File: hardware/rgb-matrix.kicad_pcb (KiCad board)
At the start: 4 copper layers, 58 x 58 mm, 84 parts, among them CON1 VEXT, P1 MATRIX_BOT, P10 PSOUTH, P11 PEAST, P12 WEST, P13 NORTH, P14 SOUTH, P15 EAST, P2 MATRIX_TOP, P3 SWD, P4 SPI3, P5 UART5, P6 VEXT, P7 USB_B, P8 PWEST, P9 PNORTH, SW1 RESET, SW2 BOOT, U1 74AC244, U2 74AC244, U3 74AC244, U4 ULN2803A, U5 STM32F405R, U6 LD3985M33R, U7 USBUF01W6, X1 8MHz

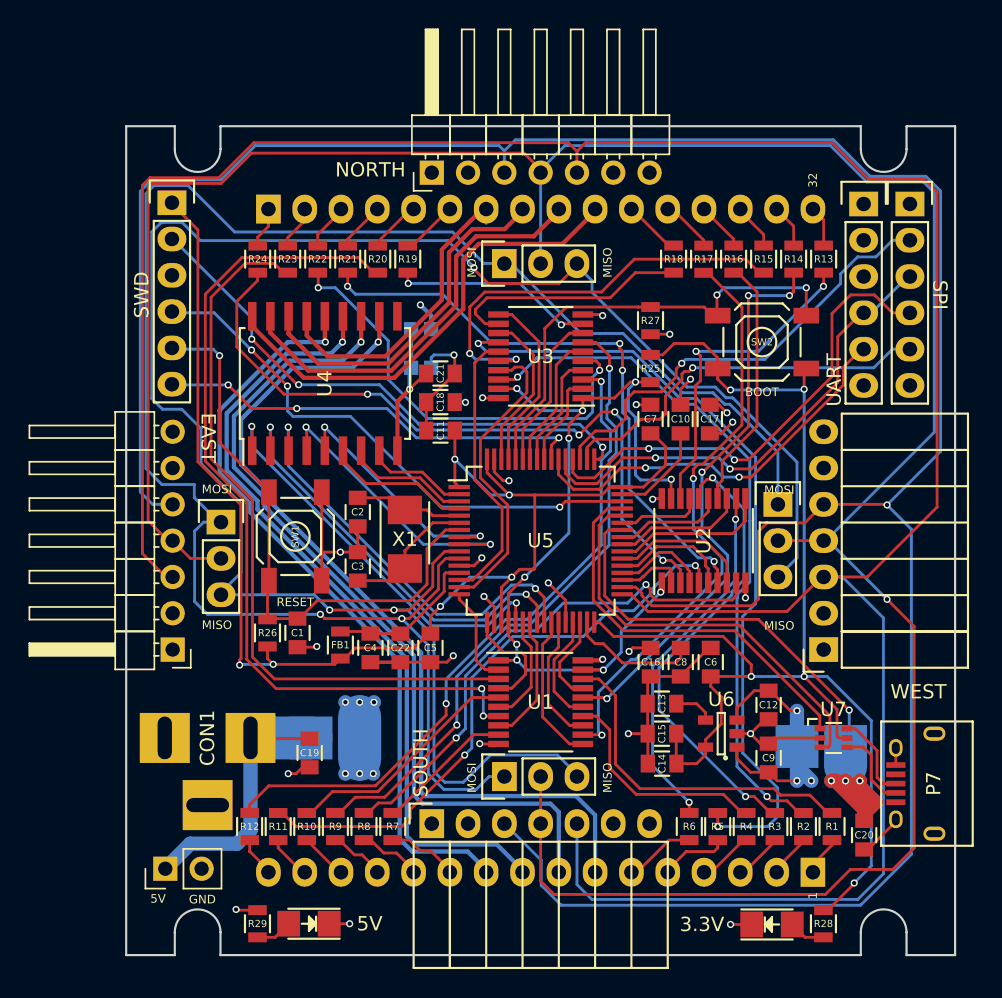
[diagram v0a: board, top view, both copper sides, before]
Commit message: Place vias on pads
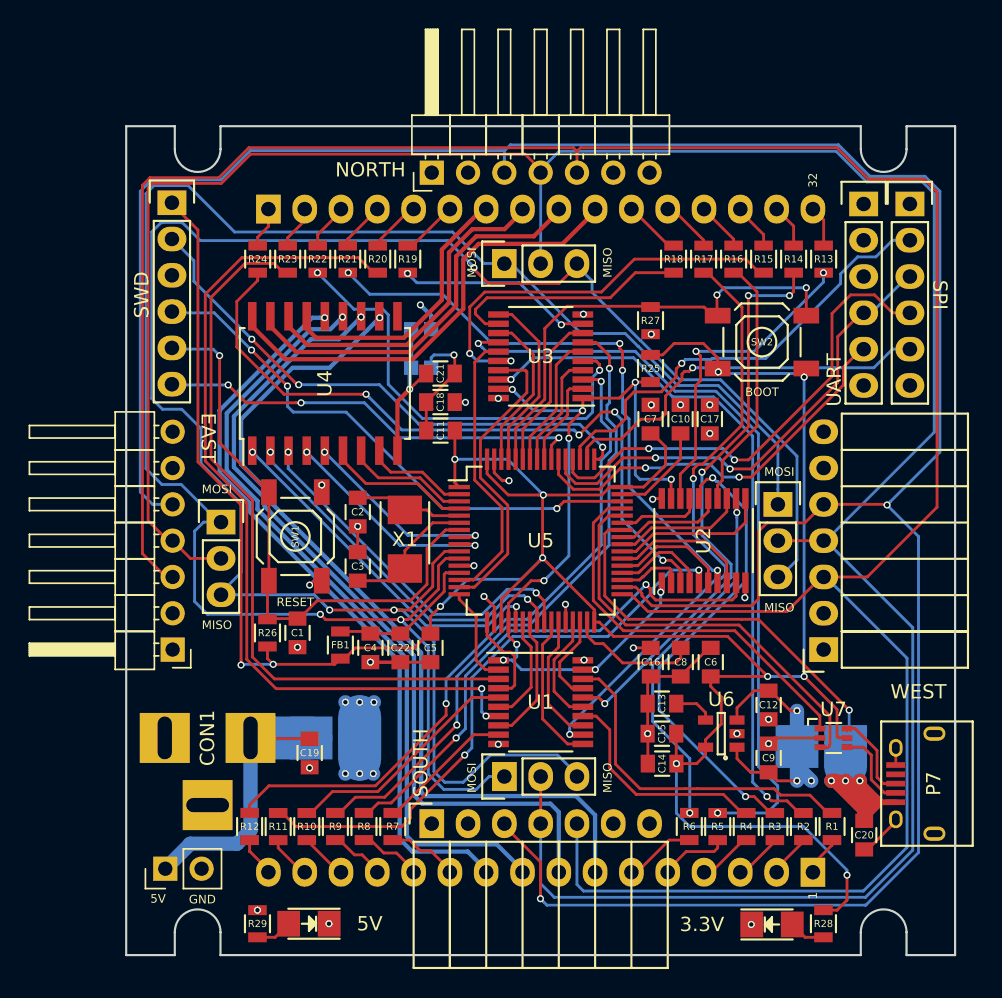
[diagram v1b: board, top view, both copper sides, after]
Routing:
- net GND: track 77.7 -> 45.6 mm, vias 20 -> 24
- net +3V3: track 187.9 -> 200.2 mm, vias 11 -> 12
- net +5V: track 44.7 -> 38.4 mm
- net ON_ROW4: track 20.8 -> 15.7 mm
- net ON_ROW3: track 30.4 -> 25.9 mm
- net ON_ROW5: track 17.9 -> 14.3 mm
- net ON_ROW1: track 28.8 -> 25.3 mm
- net ON_ROW2: track 29.4 -> 26.0 mm
- net ROW4: track 21.8 -> 19.5 mm
- net B3: track 56.1 -> 54.5 mm
- net VBUS: track 45.7 -> 47.1 mm
- net ROW3: track 25.2 -> 23.9 mm
- net ROW2: track 29.4 -> 28.0 mm
- net ROW1: track 33.6 -> 32.5 mm
- net PWM_R2: track 7.79 -> 6.73 mm
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
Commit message: PCB tweaking #1
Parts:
- moved C20 4.84 mm to (181.8, 118.0), turned to 180 degrees
- moved U7 2.83 mm to (183.5, 112.3)
- moved R15 1.85 mm to (175.9, 81.4)
- moved R21 1.85 mm to (150.5, 81.4)
- moved R13 1.85 mm to (180.1, 81.4)
- moved R14 1.85 mm to (178.0, 81.4)
- moved R16 1.85 mm to (173.8, 81.4)
- moved R17 1.85 mm to (171.7, 81.5)
- moved R18 1.85 mm to (169.6, 81.4)
- moved R19 1.85 mm to (154.7, 81.4)
- moved R20 1.85 mm to (152.6, 81.4)
- moved R22 1.85 mm to (148.4, 81.4)
- moved R23 1.85 mm to (146.3, 81.4)
- moved R24 1.85 mm to (144.2, 81.4)
- moved P15 1.24 mm to (139.8, 98.7)
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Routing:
- net +5V: track 38.4 -> 17.6 mm, vias 17 -> 23
- net VBUS: track 47.1 -> 55.0 mm, vias 4 -> 6
- net /mcu/BOOT0: track 32.9 -> 29.2 mm
- net +3V3: track 200.2 -> 196.9 mm
- net R6: track 60.5 -> 63.3 mm
- net G3: track 17.8 -> 20.1 mm, vias 0 -> 2
- net R2: track 40.8 -> 38.5 mm, vias 4 -> 2
- net Net-(P7-Pad3): track 6.26 -> 8.47 mm
- net B4: track 17.1 -> 15.0 mm
- net R4: track 41.7 -> 43.8 mm
- net B2: track 29.6 -> 27.5 mm
- net Net-(P7-Pad2): track 5.75 -> 7.74 mm
- net R8: track 51.0 -> 53.0 mm
- net G8: track 49.7 -> 51.6 mm
- net B7: track 31.3 -> 29.5 mm
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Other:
- board text added: "NRST"
- board text added: "NSS"
- board text added: "RX"
- board text added: "SCK"
- board text added: "SWCLK"
- board text added: "SWDIO"
- board text added: "SWO"
- board text added: "TX"
- board text added: "VDD"

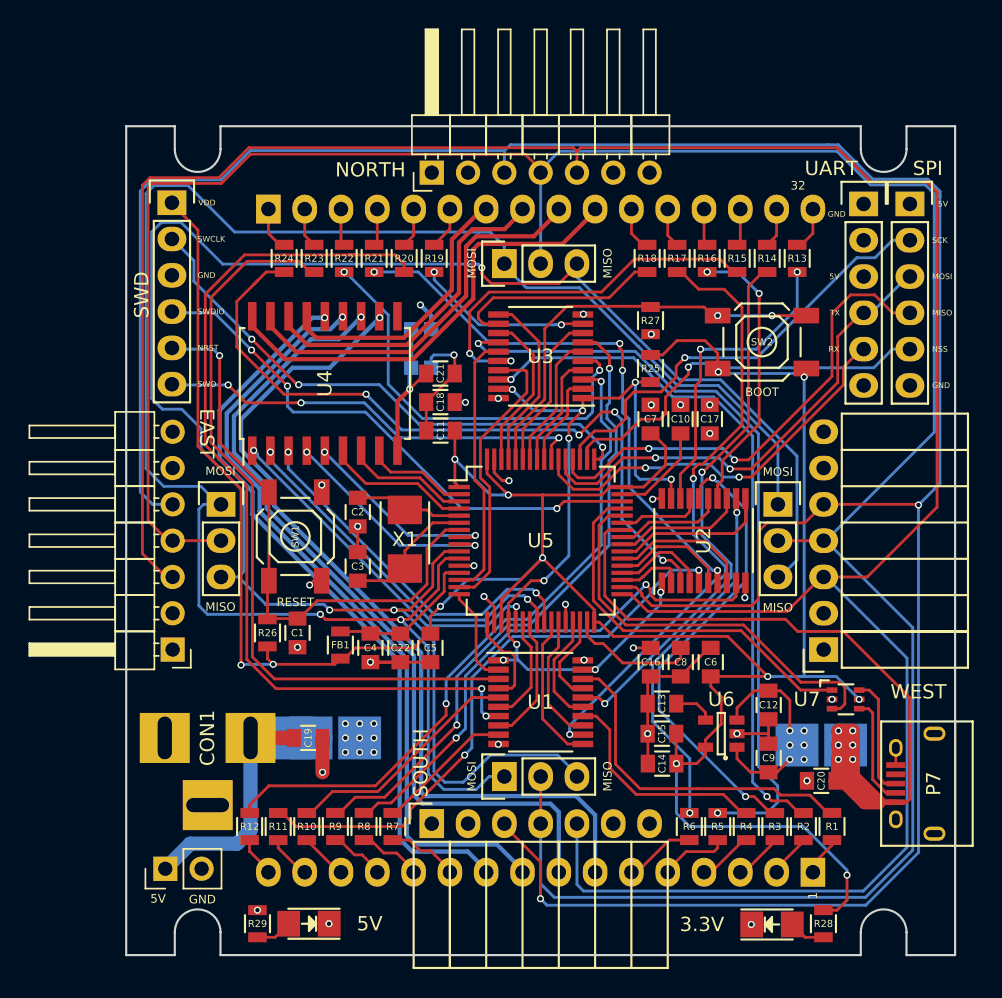
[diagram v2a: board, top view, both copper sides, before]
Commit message: Fix footprint for U7, minor other fixes
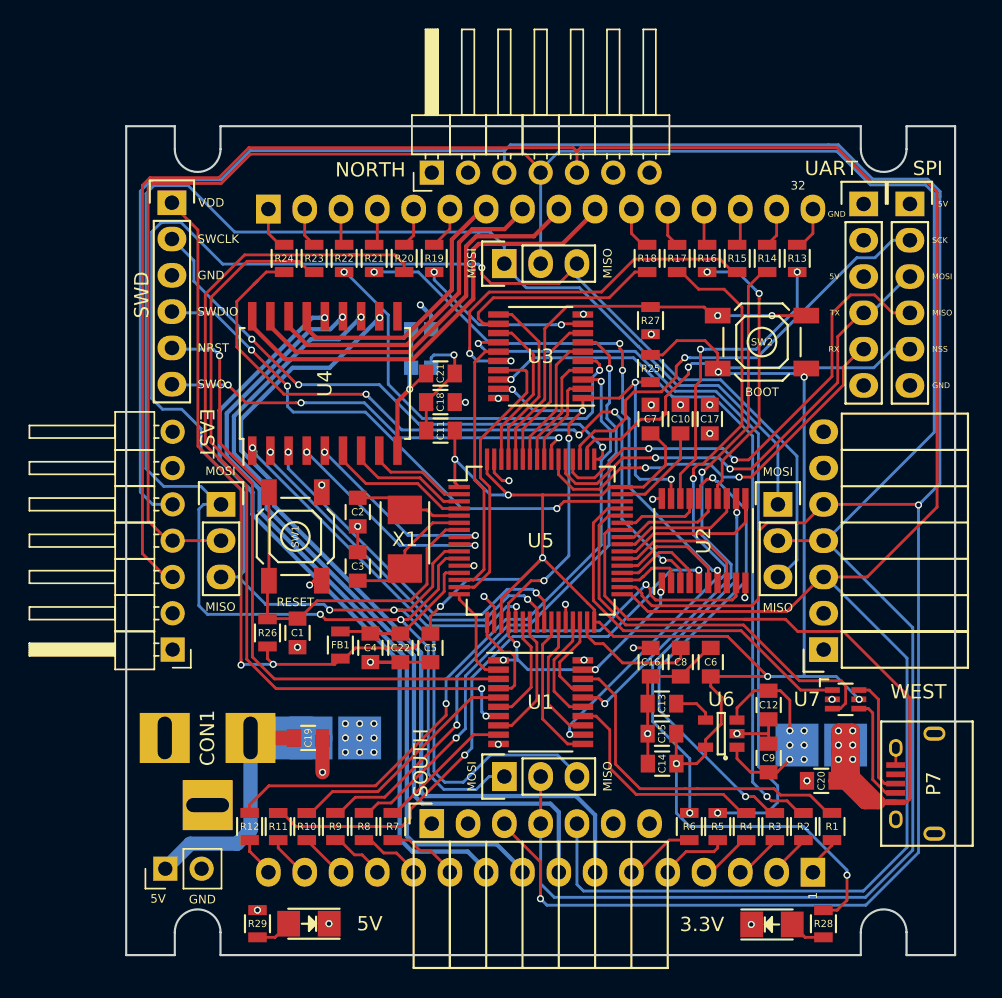
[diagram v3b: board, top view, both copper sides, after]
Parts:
- U7: footprint TO_SOT_Packages_SMD:SC-70-6 -> rgb-matrix:SOT323-6L

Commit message: Fixup silkscreen
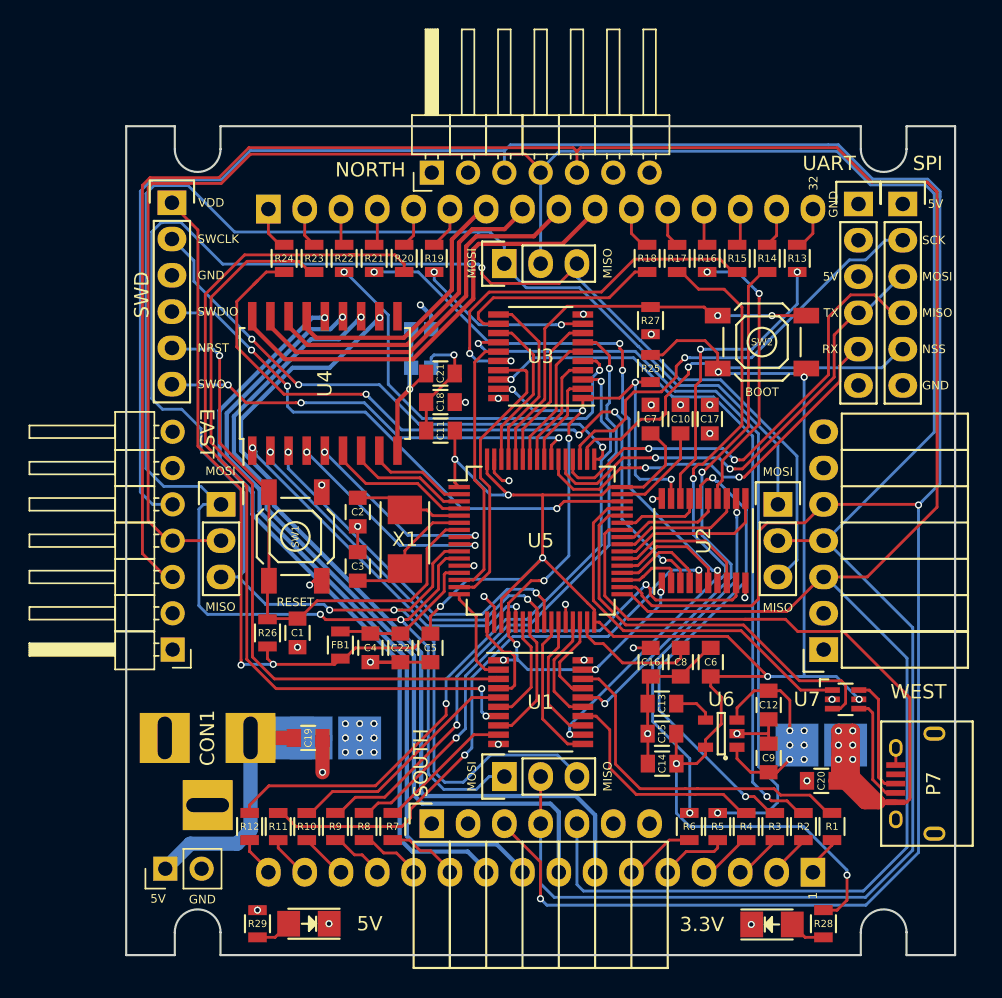
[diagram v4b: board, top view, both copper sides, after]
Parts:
- moved P4 0.50 mm to (187.5, 77.6)
- moved P5 0.36 mm to (184.4, 77.6)
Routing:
- net /mcu/SPI3_SCK: track 31.2 -> 31.9 mm
- net /mcu/SPI3_NSS: track 27.5 -> 27.0 mm
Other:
- board text added: "DATA"

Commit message: Add GND pour to Top and Bottom + via stiching
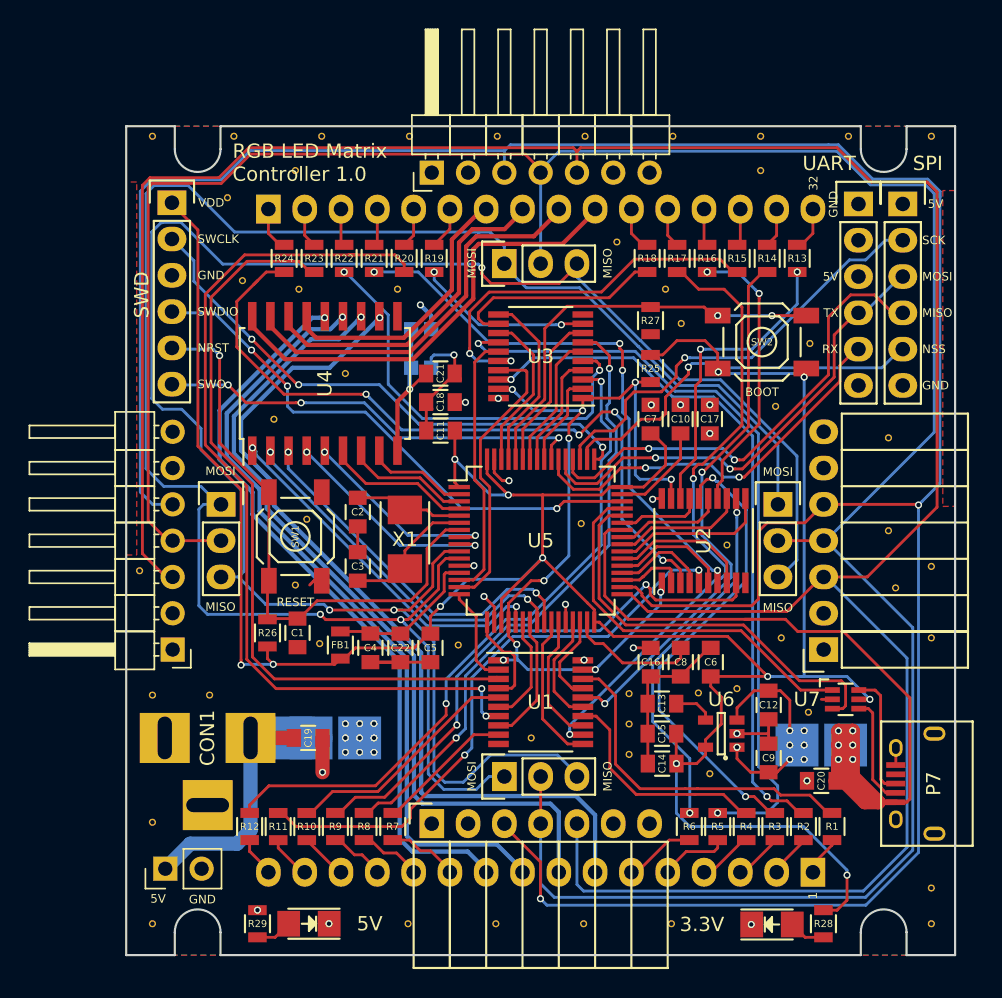
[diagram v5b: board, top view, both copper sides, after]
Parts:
- added REF**: VIA-0.5mm, VIA-0.5mm, F.Cu at (189.5, 125.5)
- added REF**: VIA-0.5mm, VIA-0.5mm, F.Cu at (181.0, 87.4)
- added REF**: VIA-0.5mm, VIA-0.5mm, F.Cu at (178.6, 91.8)
- added REF**: VIA-0.5mm, VIA-0.5mm, F.Cu at (179.0, 108.0)
- added REF**: VIA-0.5mm, VIA-0.5mm, F.Cu at (134.1, 103.3)
- added REF**: VIA-0.5mm, VIA-0.5mm, F.Cu at (135.0, 112.0)
- added REF**: VIA-0.5mm, VIA-0.5mm, F.Cu at (152.2, 83.6)
- added REF**: VIA-0.5mm, VIA-0.5mm, F.Cu at (145.2, 83.6)
- added REF**: VIA-0.5mm, VIA-0.5mm, F.Cu at (141.3, 83.0)
- added REF**: VIA-0.5mm, VIA-0.5mm, F.Cu at (180.9, 113.2)
- added REF**: VIA-0.5mm, VIA-0.5mm, F.Cu at (174.0, 117.5)
- added REF**: VIA-0.5mm, VIA-0.5mm, F.Cu at (146.7, 108.4)
- added REF**: VIA-0.5mm, VIA-0.5mm, F.Cu at (173.2, 111.8)
- added REF**: VIA-0.5mm, VIA-0.5mm, F.Cu at (168.3, 111.9)
- added REF**: VIA-0.5mm, VIA-0.5mm, F.Cu at (168.3, 114.0)
- added REF**: VIA-0.5mm, VIA-0.5mm, F.Cu at (168.3, 116.2)
- added REF**: VIA-0.5mm, VIA-0.5mm, F.Cu at (175.9, 111.5)
- added REF**: VIA-0.5mm, VIA-0.5mm, F.Cu at (148.5, 89.5)
- added REF**: VIA-0.5mm, VIA-0.5mm, F.Cu at (139.0, 112.0)
- added REF**: VIA-0.5mm, VIA-0.5mm, F.Cu at (135.0, 120.9)
- added REF**: VIA-0.5mm, VIA-0.5mm, F.Cu at (187.0, 104.5)
- added REF**: VIA-0.5mm, VIA-0.5mm, F.Cu at (189.5, 103.0)
- added REF**: VIA-0.5mm, VIA-0.5mm, F.Cu at (156.4, 108.5)
- added REF**: VIA-0.5mm, VIA-0.5mm, F.Cu at (189.5, 108.0)
- added REF**: VIA-0.5mm, VIA-0.5mm, F.Cu at (135.0, 128.0)
- added REF**: VIA-0.5mm, VIA-0.5mm, F.Cu at (152.9, 128.0)
- added REF**: VIA-0.5mm, VIA-0.5mm, F.Cu at (159.0, 128.0)
- added REF**: VIA-0.5mm, VIA-0.5mm, F.Cu at (165.2, 128.0)
- added REF**: VIA-0.5mm, VIA-0.5mm, F.Cu at (171.3, 128.0)
- added REF**: VIA-0.5mm, VIA-0.5mm, F.Cu at (189.5, 128.0)
- added REF**: VIA-0.5mm, VIA-0.5mm, F.Cu at (186.5, 94.0)
- added REF**: VIA-0.5mm, VIA-0.5mm, F.Cu at (186.5, 100.5)
- added REF**: VIA-0.5mm, VIA-0.5mm, F.Cu at (165.0, 100.0)
- added REF**: VIA-0.5mm, VIA-0.5mm, F.Cu at (161.5, 115.0)
- added REF**: VIA-0.5mm, VIA-0.5mm, F.Cu at (143.5, 92.7)
- added REF**: VIA-0.5mm, VIA-0.5mm, F.Cu at (167.5, 80.3)
- added REF**: VIA-0.5mm, VIA-0.5mm, F.Cu at (140.2, 77.2)
- added REF**: VIA-0.5mm, VIA-0.5mm, F.Cu at (145.0, 75.3)
- added REF**: VIA-0.5mm, VIA-0.5mm, F.Cu at (177.6, 75.3)
- added REF**: VIA-0.5mm, VIA-0.5mm, F.Cu at (189.5, 72.9)
- added REF**: VIA-0.5mm, VIA-0.5mm, F.Cu at (146.8, 72.9)
- added REF**: VIA-0.5mm, VIA-0.5mm, F.Cu at (177.6, 72.9)
- added REF**: VIA-0.5mm, VIA-0.5mm, F.Cu at (153.0, 72.9)
- added REF**: VIA-0.5mm, VIA-0.5mm, F.Cu at (159.1, 72.9)
- added REF**: VIA-0.5mm, VIA-0.5mm, F.Cu at (175.2, 101.5)
- added REF**: VIA-0.5mm, VIA-0.5mm, F.Cu at (165.3, 72.9)
- added REF**: VIA-0.5mm, VIA-0.5mm, F.Cu at (171.4, 72.9)
- added REF**: VIA-0.5mm, VIA-0.5mm, F.Cu at (183.7, 72.9)
- added REF**: VIA-0.5mm, VIA-0.5mm, F.Cu at (140.7, 72.9)
- added REF**: VIA-0.5mm, VIA-0.5mm, F.Cu at (135.0, 72.9)
- added REF**: VIA-0.5mm, VIA-0.5mm, F.Cu at (172.0, 86.0)
- added REF**: VIA-0.5mm, VIA-0.5mm, F.Cu at (145.8, 99.7)
- added REF**: VIA-0.5mm, VIA-0.5mm, F.Cu at (145.0, 104.3)
- added REF**: VIA-0.5mm, VIA-0.5mm, F.Cu at (170.9, 83.6)
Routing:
- net +3V3: track 196.9 -> 198.4 mm
- net GND: track 45.2 -> 44.8 mm, vias 24 -> 13
- net +5V: vias 23 -> 24
- added copper zone on B.Cu, net GND
- added copper zone on F.Cu, net GND
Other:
- board text added: "RGB LED Matrix Controller 1.0"
- board text removed: "EAST"
- board text removed: "NORTH"
- board text removed: "SOUTH"
- board text removed: "WEST"
